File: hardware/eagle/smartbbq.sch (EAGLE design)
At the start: 50 parts, among them J1 MJ_2523_SMT, J2 MJ_2523_SMT, J3 MJ_2523_SMT, J4 MJ_2523_SMT, J5 5.5od/2.1id, J6 5.5od/2.5id, J7 5.5od/2.5id, J8 22-05-7028-02, J9 22-05-7028-02, P1 CMT_1603_SMT, Q1 SSM6N58NU, U2 TLV1117-50IDCY

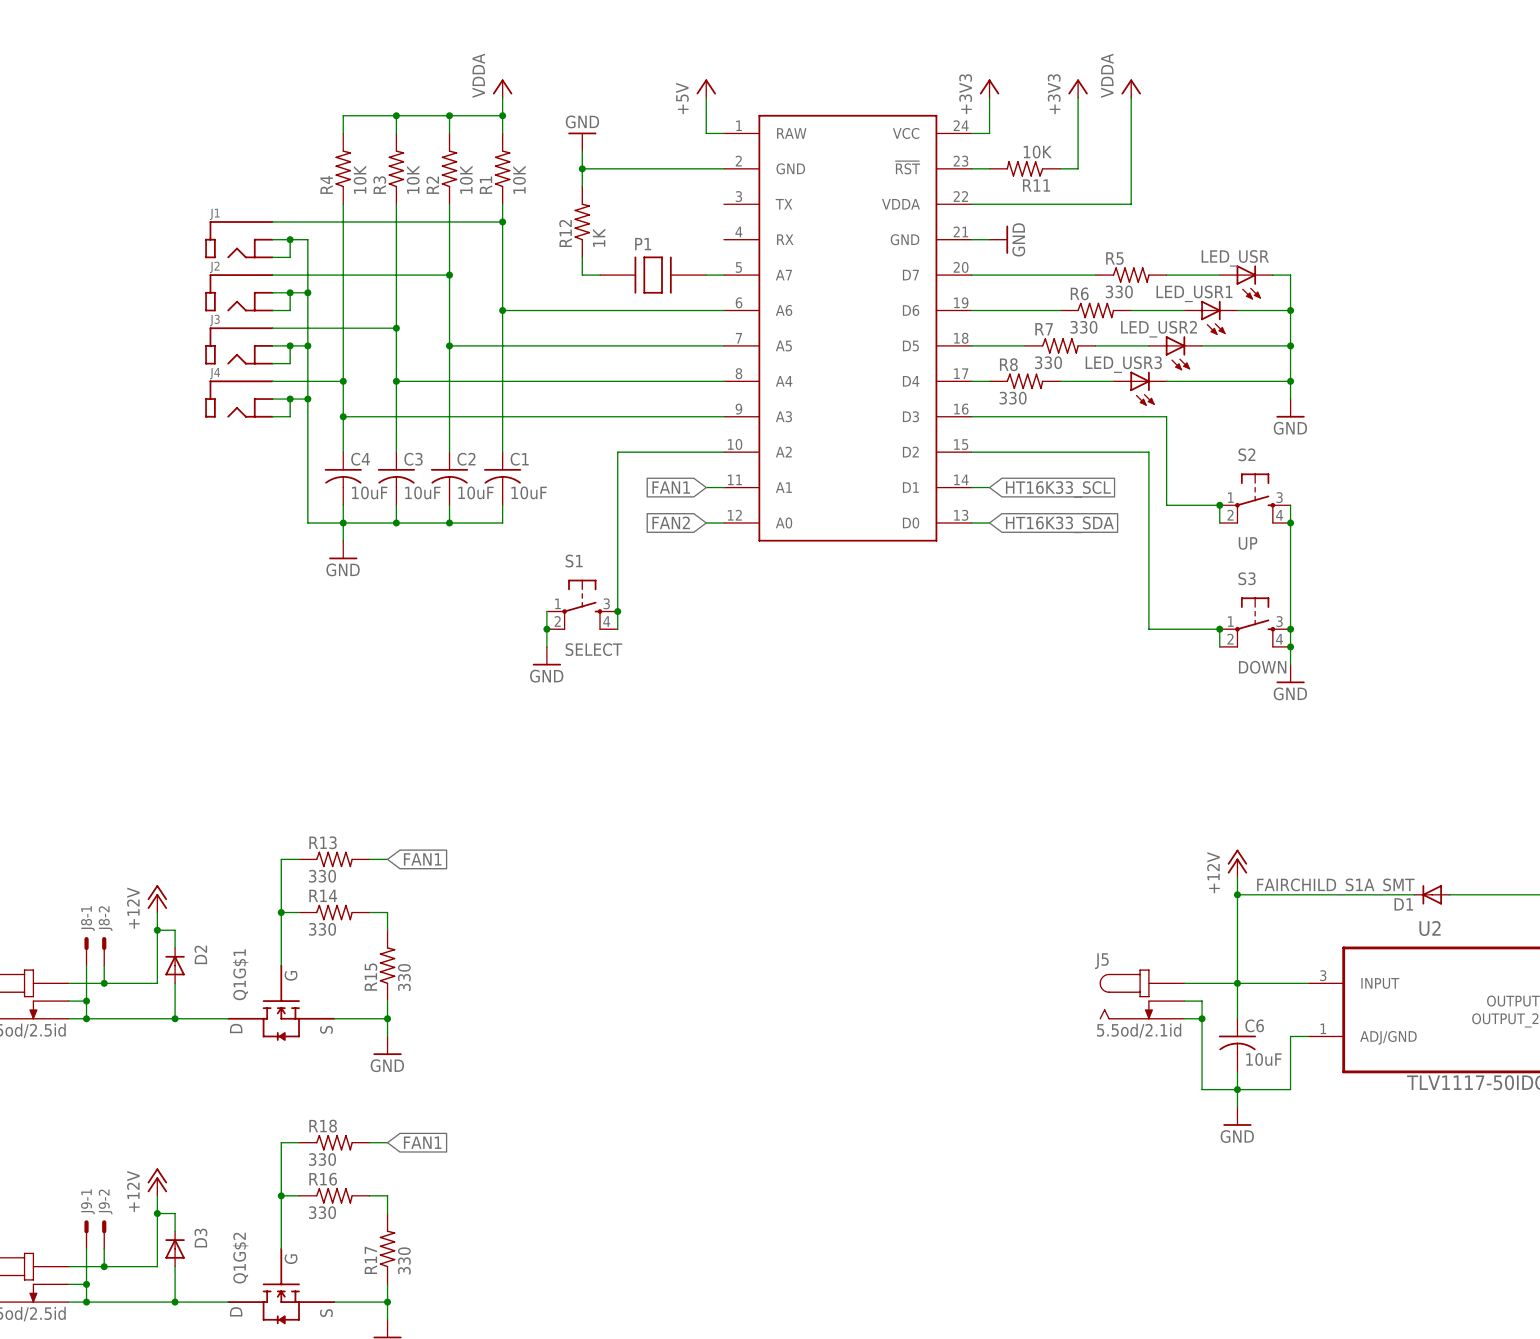
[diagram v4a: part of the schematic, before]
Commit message: Multiple updates. See description.
Looks good! I will suggest a few things though:
1.Probe inputs looks like maybe 2.5 or 3.5mm jacks. Connect the TIP to
the analog input, and the SLEEVE or RING to GND. That way ESD has a
harder path into you Spark Core inputs.

I connected the tip and NC switch to analog in and the sleeve to gnd.

2.It might be a good idea to do a Low Pass RC filter with the inputs in
a different way so that you have a resistor always in series with the
analog input. A 1k and 1uF should be plenty fast for temperature
sensors. Then you still have your 10k pull up and thermistor pulldown on
the front end. Assuming the impedance of the ADC input is high, you
won't get much of a voltage divider effect when taking a sample. The
large 1uF cap will also help this along, effectively lowering your input
impedance.

I believe I've set this up how you suggested.  Assuming I did, this will
affect my R when calcuting temp.  Should I use low tolerance(1-2%)
resistors for the 1Ks?

3.Switch inputs could use two resistors each. I know you are using the
internal pullup resistors, but ESD again can easily get to the Spark
Core inputs from something a user is purposely touching all of the time
(i.e. the switches). Minimum 1k series, 10k pull up. Put the pull up at
the switch, not the Core, that way the switch can pull it all of the way
to ground.

Makes sense and sounds like a good best practice. I have updated.

4.I would add a diode in series right after the J6 output (input power),
just in case anyone decides to plug in a reverse polarity wall adapter.
Also a polyfuse in series with the diode.

I'm thinking you mean right after J5 input, in which case I have added
them and that totally makes sense.  Hopefully I'm not misunderstanding.

5.R18 should connect to FAN2, not FAN1 (copy/paste error wink )

Bah, fixed :)

6.I would make the fan connectors whatever the fans normally come with
to save cost... whatever you use make sure the connections are not
exposed before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
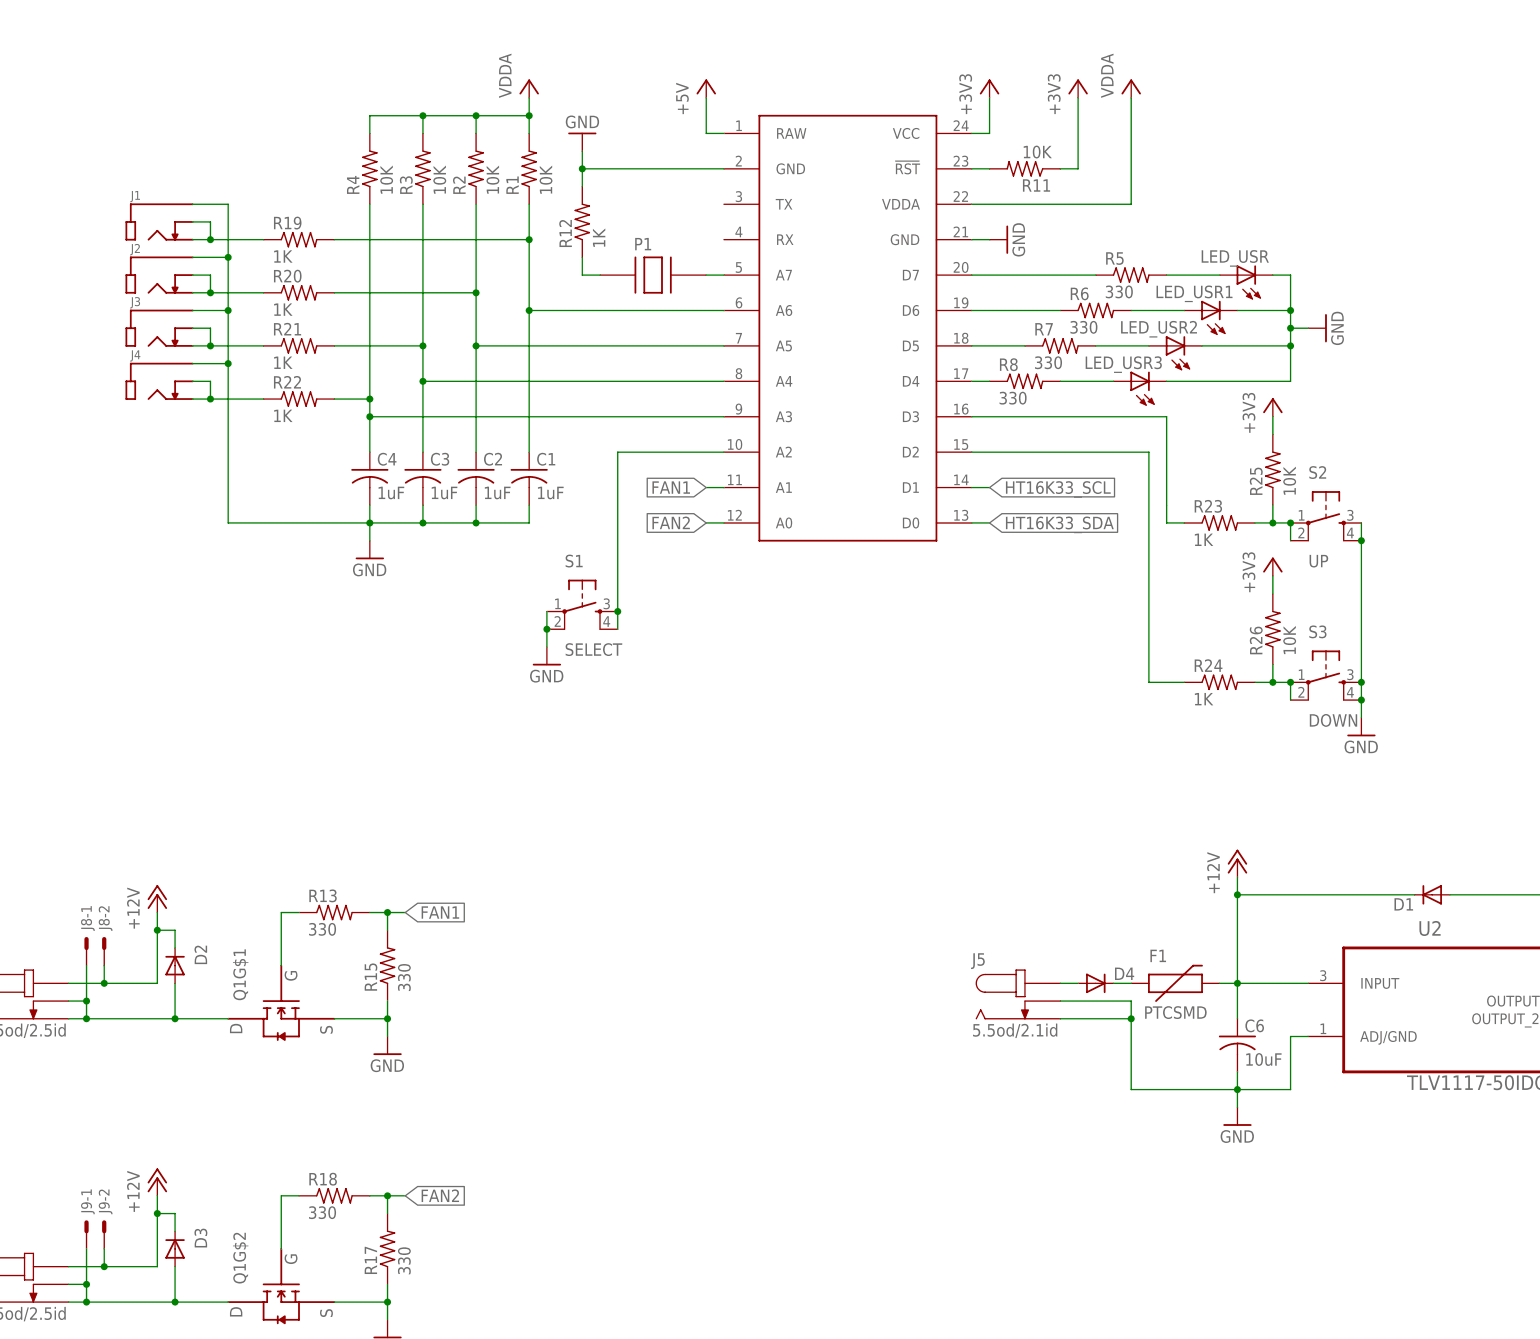
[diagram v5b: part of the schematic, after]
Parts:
- removed R14, R16: 330, rcl:R-US_R0805
- added D4: FAIRCHILD_S1A_SMT, engirati:FAIRCHILD_S1A_SMT
- added F1: PTCSMD, SparkFun-PowerIC:PTCSMD
- added R19, R20, R21, R22, R23, R24: 1K, rcl:R-US_R0805
- added R25, R26: 10K, rcl:R-US_R0805
- C1, C2, C3, C4: value 10uF -> 1uF
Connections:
- removed net N$35: R14.2, R15.2
- new net N$36: J4.P$2, J4.P$3, R22.1
- new net N$37: J3.P$2, J3.P$3, R21.1
- new net N$38: J2.P$2, J2.P$3, R20.1
- new net N$39: J1.P$2, J1.P$3, R19.1
- new net N$40: R23.2, R25.1, S2.1, S2.2
- new net N$41: D4.A, J5.P$1
- new net N$42: R24.2, R26.1, S3.1, S3.2
- net +12V: now also F1.2; no longer J5.P$1
- net +3V3: now also R25.2, R26.2
- net FAN1: now also R15.2; no longer R18.2
- net FAN2: now also R17.2, R18.2
- net GND: now also J1.P$1, J2.P$1, J3.P$1, J4.P$1; no longer J1.P$2, J1.P$3, J2.P$2, J2.P$3, J3.P$2, J3.P$3, J4.P$2, J4.P$3
- net N$13: now also R24.1; no longer S3.1, S3.2
- net N$14: now also R23.1; no longer S2.1, S2.2
- net N$15: now also R19.2; no longer J1.P$1
- net N$17: now also R20.2; no longer J2.P$1
- net N$18: now also R21.2; no longer J3.P$1
- net N$19: now also R22.2; no longer J4.P$1
- net N$31: no longer R16.1
- net N$33: now also D4.C, F1.1; no longer R16.2, R17.2
- net N$34: no longer R14.1
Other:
- moved on the sheet: C1, C2, C3, C4, J5, R1, R13, R18, R2, R3, R4, S2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
